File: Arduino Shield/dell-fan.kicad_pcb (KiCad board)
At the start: 2 copper layers, 101.6 x 53.3 mm, 50 parts, among them J1 Power, P1 Digital, P10 CONN_01X01, P11 CONN_01X01, P13 CONN_01X01, P2 Power, P3 Analog, P4 Analog, P5 PWM, P6 PWM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

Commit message: making resistors larger
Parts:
- R1, R10, R11, R12, R2, R3, R4, R5, R6, R7, R8, R9: footprint Resistor_THT:R_Box_L8.4mm_W2.5mm_P5.08mm -> Resistor_THT:R_Box_L13.0mm_W4.0mm_P9.00mm
- moved R10 1.27 mm to (175.3, 85.1)
- moved R12 1.27 mm to (188.0, 85.1)
- moved R2 1.27 mm to (123.2, 85.1)
- moved R4 1.27 mm to (137.2, 85.1)
- moved R6 1.27 mm to (149.9, 85.1)
- moved R8 1.27 mm to (162.6, 85.1)
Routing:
- net FAN5_TACH: track 11.2 -> 5.96 mm
- net FAN2_TACH: track 11.6 -> 6.38 mm
- net FAN3_TACH: track 13.5 -> 9.53 mm
- net FAN6_TACH: track 13.9 -> 10.5 mm
- net FAN4_TACH: track 16.3 -> 14.5 mm
- net +5V: track 86.2 -> 87.6 mm
- net FAN1_TACH: track 18.5 -> 17.1 mm

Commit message: removing ground link from pcb design
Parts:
- removed GND_LNK1: GND, Connector_PinHeader_2.54mm:PinHeader_1x01_P2.54mm_Vertical

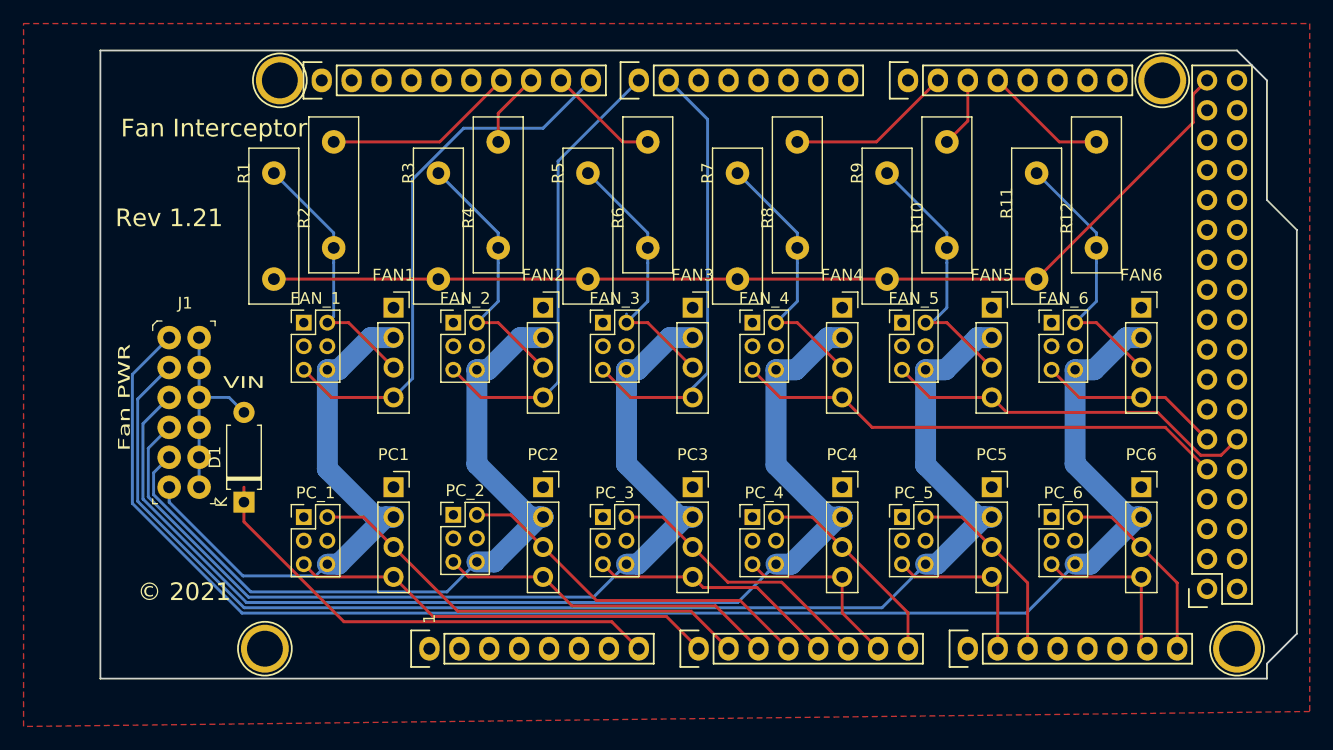
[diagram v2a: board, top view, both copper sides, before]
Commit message: redesign for rev 2.01.  Swapped PC and FAN location, and swapped FAN4_PWM and FAN5_PWM pins for simplicity
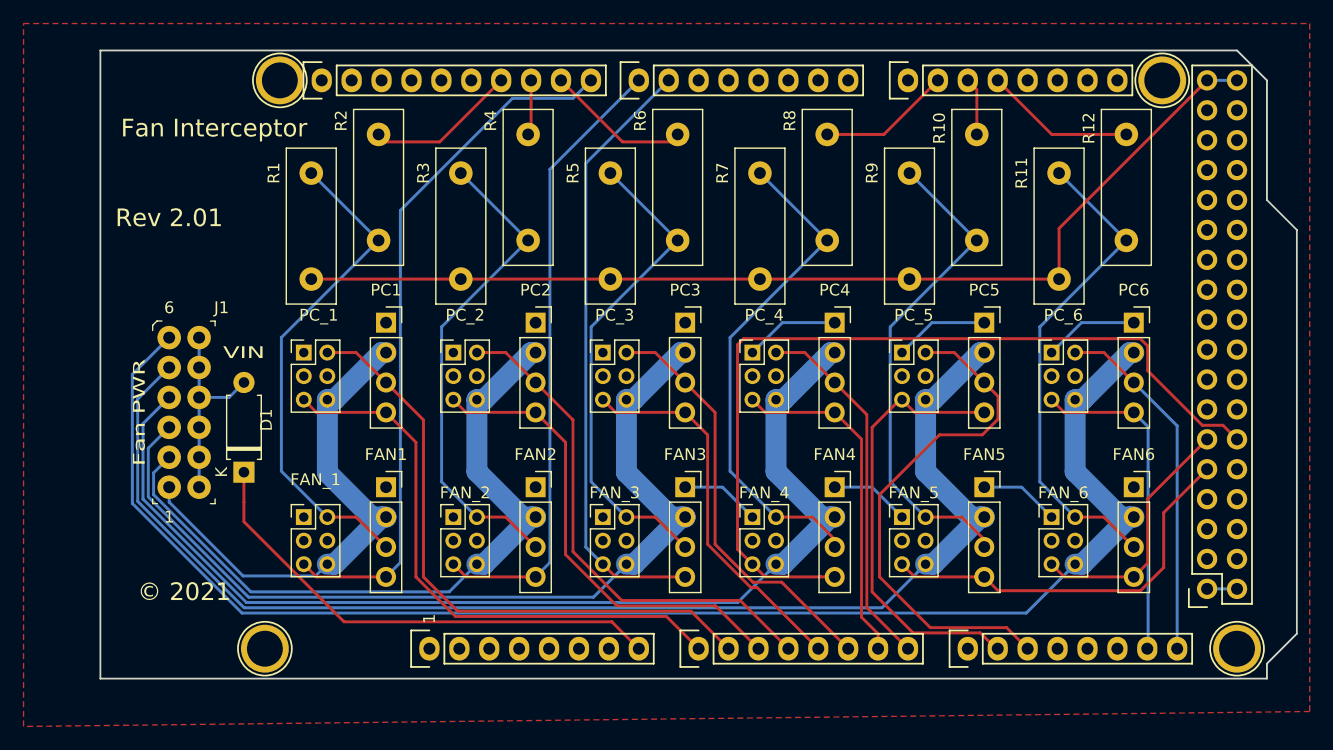
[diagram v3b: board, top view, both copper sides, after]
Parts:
- moved FAN_1 16.5 mm to (120.7, 108.0)
- moved FAN_2 16.5 mm to (133.3, 108.0)
- moved FAN_3 16.5 mm to (146.1, 108.0)
- moved FAN_4 16.5 mm to (158.8, 108.0)
- moved FAN_5 16.5 mm to (171.4, 108.0)
- moved FAN_6 16.5 mm to (184.2, 108.0)
- moved FAN1 15.3 mm to (127.6, 105.4)
- moved FAN2 15.3 mm to (140.3, 105.4)
- moved FAN3 15.3 mm to (153.0, 105.4)
- moved FAN4 15.3 mm to (165.7, 105.4)
- moved FAN5 15.3 mm to (178.4, 105.4)
- moved FAN6 15.3 mm to (191.1, 105.4)
- moved PC1 14.0 mm to (127.6, 91.4)
- moved PC2 14.0 mm to (140.3, 91.4)
- moved PC3 14.0 mm to (153.0, 91.4)
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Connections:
- P1 pad 12: FAN5_PWM -> FAN4_PWM
- P1 pad 9: FAN4_PWM -> FAN5_PWM
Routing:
- net GND: track 0.00 -> 47.0 mm
- net FAN4_PWM: track 42.1 -> 74.0 mm
- net PC5_TACH: track 16.6 -> 44.4 mm
- net PC5_PWM: track 14.4 -> 37.6 mm
- net FAN1_TACH_IN: track 22.2 -> 43.3 mm
- net FAN4_TACH_IN: track 22.8 -> 43.3 mm
- net FAN5_TACH_IN: track 23.1 -> 43.2 mm
- net FAN2_TACH_IN: track 22.8 -> 42.5 mm
- net FAN6_TACH_IN: track 22.8 -> 41.9 mm
- net FAN3_TACH_IN: track 23.5 -> 41.9 mm
- net FAN3_PWM: track 37.4 -> 52.0 mm
- net PC6_PWM: track 14.4 -> 28.7 mm
- net FAN2_PWM: track 38.9 -> 53.2 mm
- net PC1_TACH: track 38.7 -> 52.3 mm
- net PC4_PWM: track 15.4 -> 29.0 mm
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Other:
- board text added: "6"
- board text added: "Rev 2.01"
- board text removed: "Rev 1.21"
